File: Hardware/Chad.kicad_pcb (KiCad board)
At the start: 4 copper layers, 30 x 60 mm, 131 parts, among them J1 RBUS, J2 GPIO Breakout, J3 ServoCH1, J4 ServoCH2, J5 USB_C_Receptacle_USB2.0, Q1 SSM3K15AMFV,L3F, U1 ESP32-S3, U2 SN65HVD230, U3 LM66200DRLR, U4 MAX77827AEFD+T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

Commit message: Maybe chad v3.0 hardware
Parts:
- added C18: TBD, Capacitor_SMD:C_0603_1608Metric, B.Cu at (49.9, 89.7)
- added C19: 47uF, Capacitor_SMD:C_1206_3216Metric, B.Cu at (59.2, 90.6)
- added D3: ~, Package_TO_SOT_SMD:SOT-353_SC-70-5, B.Cu at (50.4, 74.0)
- added R40: TBD, Resistor_SMD:R_0402_1005Metric, B.Cu at (52.5, 75.6)
- added R41: TBD, Resistor_SMD:R_0402_1005Metric, B.Cu at (51.9, 76.2)
- added R42: TBD, Resistor_SMD:R_0603_1608Metric, B.Cu at (49.2, 86.8)
- C12: value 4.2pF -> DNP
- C13, C14: value C -> 11pF
- C31, C34, C36, C40, C41, C42, C43, C44, C47, C49: value DNP -> 47uF
- C46: value DNP -> 47uF; footprint Capacitor_SMD:C_0805_2012Metric -> Capacitor_SMD:C_1206_3216Metric; moved to B.Cu
- C48: value DNP -> 47uF; footprint Capacitor_SMD:C_0805_2012Metric -> Capacitor_SMD:C_1206_3216Metric
- R13: value 470 -> 5.1k
- R28, R29, R30, R31, R32, R33: value DNP -> 10k
- R5: value 47.5 -> DNP
- U6: value SiC437BED-T1-GE3 -> SiC437AED-T1
- Y1: value 40MHz±10ppm -> R940000171
- moved SERVOLED1 2.43 mm to (53.9, 76.3), turned to -90 degrees
- moved C47 1.46 mm to (59.2, 93.0)
- moved C49 1.45 mm to (59.2, 90.7)
- moved LOGO1 1.43 mm to (49.6, 80.5)
- moved R25 1.40 mm to (53.9, 78.2), turned to 90 degrees
- moved C46 1.25 mm to (59.2, 93.0)
- moved J4 0.96 mm to (55.8, 81.7)
- moved C48 0.71 mm to (52.7, 93.1)
- moved C17 0.46 mm to (34.8, 62.1), turned to -90 degrees
- moved C16 0.36 mm to (42.4, 66.5)
- moved C15 0.36 mm to (42.4, 65.5)
- moved R10 0.33 mm to (37.4, 62.3)
- moved R9 0.33 mm to (37.4, 60.9)
- moved J3 0.26 mm to (55.8, 71.0)
- moved CANTXLED1 0.20 mm to (39.0, 64.3)
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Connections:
- net +12V renamed +16.8V
- net /GPIO0 renamed /GPIO10
- net /GPIO1 renamed /GPIO8
- net /GPIO2 renamed /GPIO9
- net /GPIO3 renamed /GPIO7
- J2 pad 7: /GPIO4 -> /GPIO5
- J2 pad 8: /GPIO5 -> /GPIO6
- J3 pad 3: /Servo1PWM -> Net-(J3-Pin_3)
- J4 pad 3: /Servo2PWM -> Net-(J4-Pin_3)
- R32 pad 2: /GPIO4 -> /GPIO5
- R33 pad 2: /GPIO5 -> /GPIO6
- U1 pad 10: /GPIO4 -> /GPIO5
- U1 pad 11: /GPIO5 -> /GPIO6
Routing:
- net /GPIO4: track 13.6 -> 0.00 mm
- net Net-(J4-Pin_3): track 0.00 -> 12.4 mm
- net /Servo2PWM: track 27.5 -> 16.6 mm
- net /GPIO6: track 0.00 -> 8.12 mm
- net /GPIO5: track 8.12 -> 13.6 mm
- net /Servo1PWM: track 20.9 -> 17.4 mm
- net Net-(J3-Pin_3): track 0.00 -> 3.02 mm
- net +6V: track 17.1 -> 14.3 mm
- net +3V3: track 34.9 -> 32.6 mm
- net /CAN_TX: track 7.48 -> 8.43 mm
- net /buckC/SW: track 0.00 -> 0.81 mm, vias 0 -> 1
- net /CAN-: track 26.8 -> 26.0 mm
- added copper zone on B.Cu, net Net-(C18-Pad2)
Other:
- board text added: "C.H.A.D v3.0"
- board text added: "Designed By Andrei Paduraru Electronics 2024"
- board text removed: "C.H.A.D v2.0"
- board text removed: "Designed By Andrei Paduraru Electronics and Payload 2023"

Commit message: RAE logo
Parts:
- added G***: LOGO, iclr:rae_logo_4mm, F.Cu at (35.5, 93.0)

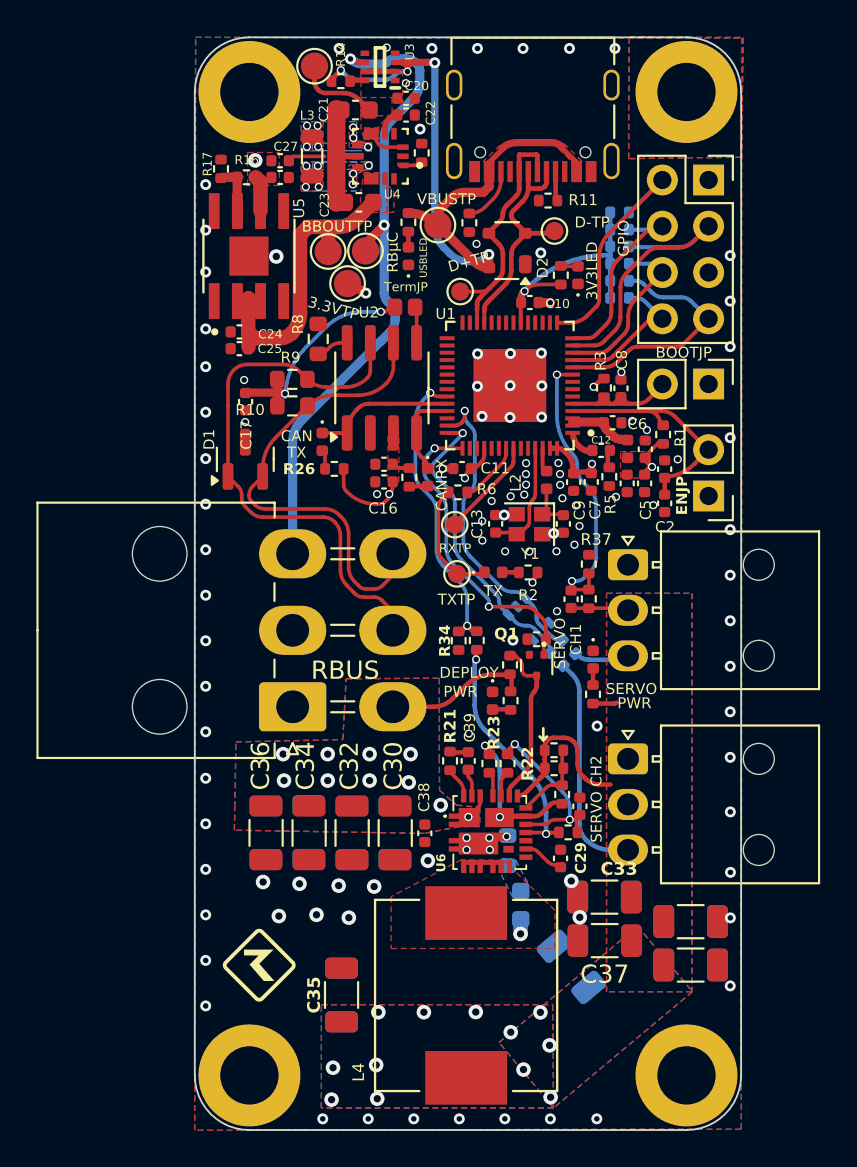
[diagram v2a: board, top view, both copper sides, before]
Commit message: 30V compatibility update
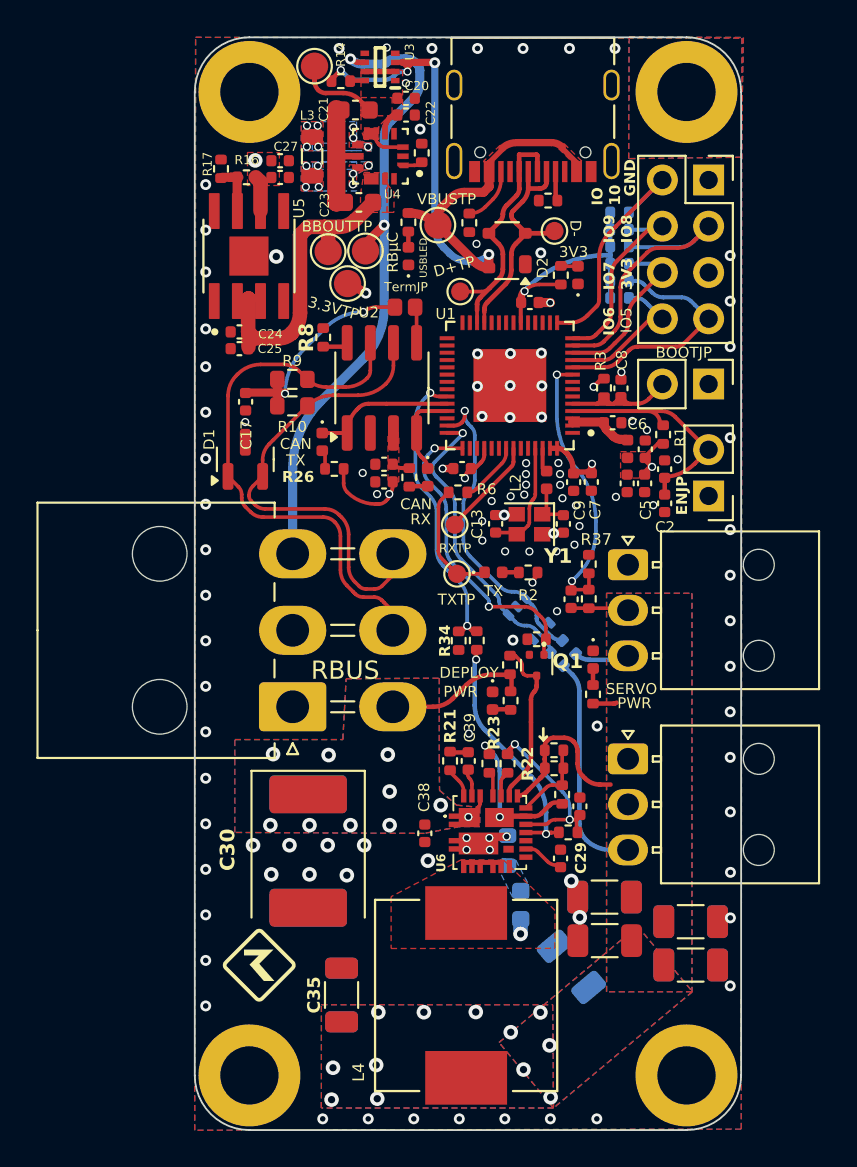
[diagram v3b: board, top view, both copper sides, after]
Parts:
- removed C12: DNP, Capacitor_SMD:C_0402_1005Metric
- removed C34, C36, C41, C42, C43, C44: 47uF, Capacitor_SMD:C_1206_3216Metric
- removed R5: DNP, Resistor_SMD:R_0402_1005Metric
- 12VLED1: value 12V_LED -> RED_LED
- 3V3LED1: value 3V3LED -> BLUE_LED
- C30: value 47uF -> 100uF; footprint Capacitor_SMD:C_1206_3216Metric -> Capacitor_Tantalum_SMD:CP_EIA-7360-38_Kemet-E
- C32: value 47uF -> 100uF; footprint Capacitor_SMD:C_1206_3216Metric -> Capacitor_Tantalum_SMD:CP_EIA-7360-38_Kemet-E; moved to B.Cu
- CANRXLED1: value CANRXLED -> AMBER_LED
- CANTXLED1: value CANTXLED -> GREEN_LED
- J1: footprint Connector_Molex:Molex_Mini-Fit_Jr_5569-06A2_2x03_P4.20mm_Horizontal -> iclr:Molex_Mini-Fit_Jr_5569-06A2_2x03_P4.20mm_Horizontal
- J3, J4: footprint Connector_Molex:Molex_Nano-Fit_105313-xx03_1x03_P2.50mm_Horizontal -> iclr:Molex_Nano-Fit_105313-xx03_1x03_P2.50mm_Horizontal
- J5: footprint Connector_USB:USB_C_Receptacle_Palconn_UTC16-G -> iclr:USB_C_Receptacle_Palconn_UTC16-G
- Q1: footprint Package_TO_SOT_SMD:SOT-723 -> iclr:SOT-723
- R8: footprint Resistor_SMD:R_0603_1608Metric -> Resistor_SMD:R_0402_1005Metric
- SERVOLED1: value 6V_LED -> AMBER_LED
- TXLED1: value TX_LED -> GREEN_LED
- U5: value SC4215 -> SC4215ASTRT
- USBLED1: value USB_LED -> WHITE_LED
- Y1: footprint Crystal:Crystal_SMD_2016-4Pin_2.0x1.6mm -> iclr:Crystal_SMD_2016-4Pin_2.0x1.6mm
- moved C30 4.88 mm to (38.2, 86.8)
- moved C32 2.61 mm to (38.2, 86.8)
- moved R8 0.28 mm to (39.0, 58.6)
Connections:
- U1 pad 1: Net-(U1-LNA_IN/RF) -> unconnected-(U1-LNA_IN/RF-Pad1)
- U5 pad 5: (no net) -> unconnected-(U5-NC-Pad5)
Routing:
- net GND: track 19.0 -> 16.9 mm
- net Net-(U1-LNA_IN/RF): track 1.54 -> 0.00 mm
- net Net-(C12-Pad1): track 0.91 -> 0.00 mm
- net /CAN+: track 30.7 -> 31.6 mm
- net RBUS_uC_V: track 36.6 -> 35.8 mm
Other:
- board text added: "GND"
- board text added: "ID"
- board text added: "IO 10"
- board text added: "IO6"
- board text added: "IO7 3V3"
- board text added: "IO9 IO8"
- board text removed: "Board Number -"

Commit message: Resistor values
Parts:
- R19: value 130k -> 113k
- R24: value 294k -> 442k
- R40, R41: value TBD -> 165R
